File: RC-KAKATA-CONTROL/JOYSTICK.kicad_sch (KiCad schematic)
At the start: 5 parts, among them U4 YK16S-L7.2-B10KA(32-8)-G-A29

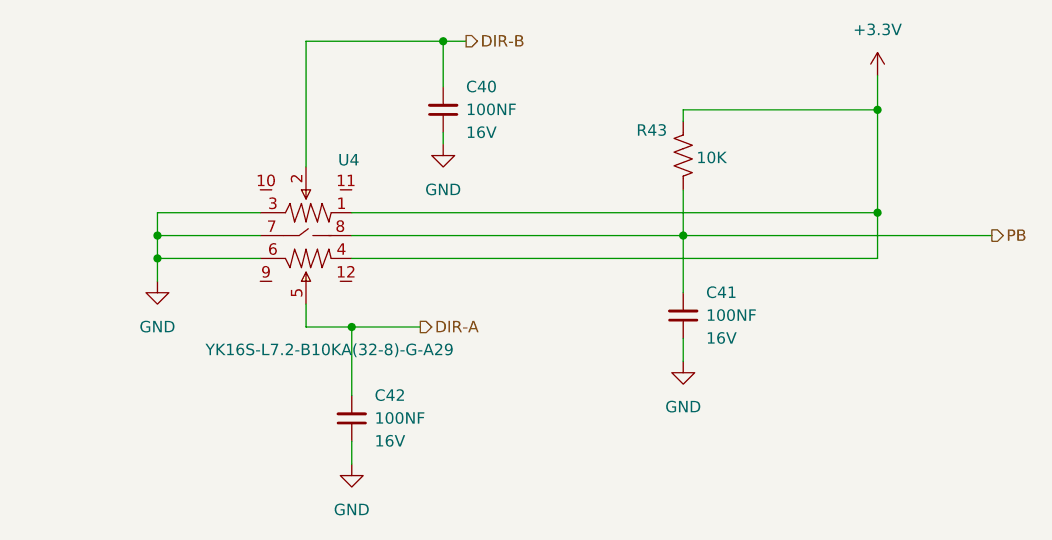
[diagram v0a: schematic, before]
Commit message: Agregadas conexiones de analogicos Agregadas las conexiones de i2c Agregadas las conexiones de Uart Cambiados algunos detalles de tvs resistencias y cap Recolocados los componenetes de power supply Cambiados los diodos de entrada de la bateria por unos de 5A Cambios menores y mejorada la documentacion Agregada informacion en la serigrafia del PCB
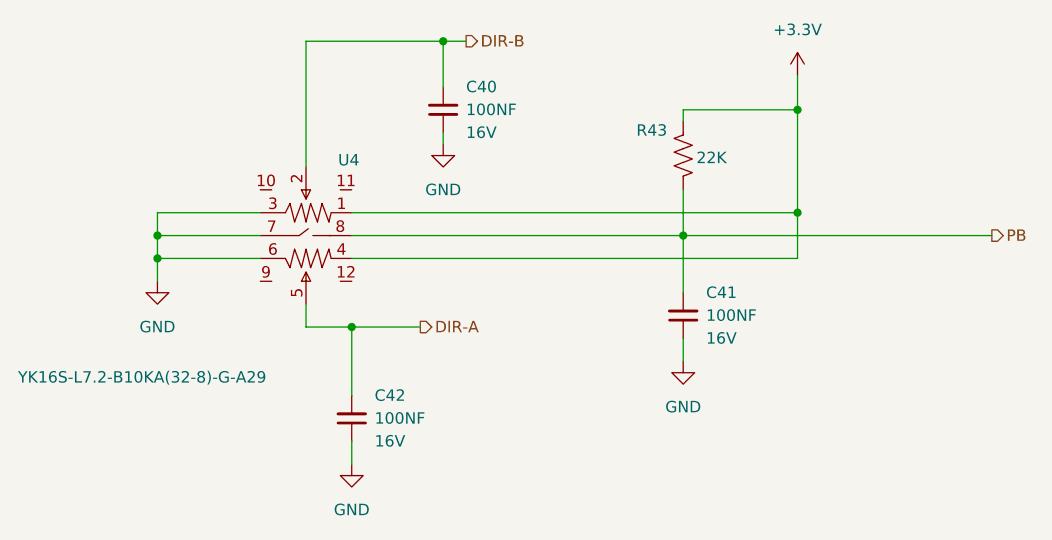
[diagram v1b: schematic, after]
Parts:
- R43: value 10K -> 22K
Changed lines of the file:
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@@
 	)
 	(junction
-		(at 158.75 83.82)
+		(at 149.86 83.82)
 		(diameter 0)
 		(color 0 0 0 0)
@@
 	)
 	(junction
-		(at 158.75 72.39)
+		(at 149.86 72.39)
 		(diameter 0)
 		(color 0 0 0 0)
@@
 	(wire
 		(pts
-			(xy 100.33 88.9) (xy 158.75 88.9)
+			(xy 100.33 88.9) (xy 149.86 88.9)
 		)
 		(stroke
@@
 	(wire
 		(pts
-			(xy 137.16 72.39) (xy 158.75 72.39)
+			(xy 137.16 72.39) (xy 149.86 72.39)
 		)
 		(stroke
@@
 	(wire
 		(pts
-			(xy 158.75 88.9) (xy 158.75 83.82)
-		)
-		(stroke
-			(width 0)
-			(type default)
-		)
-	)
-	(wire
-		(pts
-			(xy 158.75 68.58) (xy 158.75 72.39)
+			(xy 149.86 88.9) (xy 149.86 83.82)
+		)
+		(stroke
+			(width 0)
+			(type default)
+		)
+	)
+	(wire
+		(pts
+			(xy 149.86 68.58) (xy 149.86 72.39)
 		)
 		(stroke
@@
 	(wire
 		(pts
-			(xy 100.33 83.82) (xy 158.75 83.82)
+			(xy 100.33 83.82) (xy 149.86 83.82)
 		)
 		(stroke
@@
 	(wire
 		(pts
-			(xy 158.75 72.39) (xy 158.75 83.82)
+			(xy 149.86 72.39) (xy 149.86 83.82)
 		)
 		(stroke
@@
 			)
 		)
-		(property "Value" "10K"
+		(property "Value" "22K"
 			(at 141.986 77.724 0)
 			(effects
@@
 		)
 		(property "Value" "YK16S-L7.2-B10KA(32-8)-G-A29"
-			(at 84.074 99.06 0)
+			(at 63.246 102.108 0)
 			(effects
 				(font
@@
 	(symbol
 		(lib_id "power:+3.3V")
-		(at 158.75 68.58 0)
+		(at 149.86 68.58 0)
 		(unit 1)
 		(exclude_from_sim no)
@@
 		(fields_autoplaced yes)
 		(property "Reference" "#PWR107"
-			(at 158.75 72.39 0)
+			(at 149.86 72.39 0)
 			(effects
 				(font
@@
 		)
 		(property "Value" "+3.3V"
-			(at 158.75 63.5 0)
+			(at 149.86 63.5 0)
 			(effects
 				(font
@@
 		)
 		(property "Footprint" ""
-			(at 158.75 68.58 0)
+			(at 149.86 68.58 0)
 			(effects
 				(font
@@
 		)
 		(property "Datasheet" ""
-			(at 158.75 68.58 0)
+			(at 149.86 68.58 0)
 			(effects
 				(font
@@
 		)
 		(property "Description" "Power symbol creates a global label with name \"+3.3V\""
-			(at 158.75 68.58 0)
-			(effects
-				(font
+			(at 149.86 68.58 0)
+			(effects
+				(font

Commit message: Colocadas todas las piezas Verificacion de conexiones de los puertos UART - I2C - SPI Realizadas todas las conexiones Verificados los errores
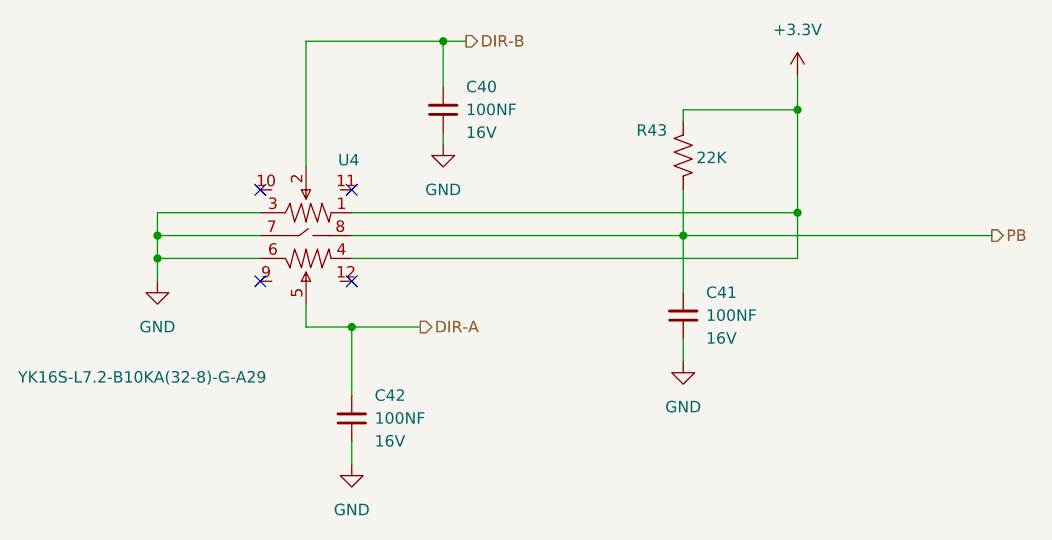
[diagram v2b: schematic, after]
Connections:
- no-connect marks 0 -> 4
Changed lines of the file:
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@@
 	(generator "eeschema")
 	(generator_version "9.0")
-	(paper "A4")
+	(paper "USLedger")
 	(title_block
 		(title "RC-KAKATA-CONTROL")
@@
 		(color 0 0 0 0)
 	)
+	(no_connect
+		(at 100.33 81.28)
+	)
+	(no_connect
+		(at 90.17 91.44)
+	)
+	(no_connect
+		(at 100.33 91.44)
+	)
+	(no_connect
+		(at 90.17 81.28)
+	)
 	(wire
